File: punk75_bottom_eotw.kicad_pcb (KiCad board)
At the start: 2 copper layers, 285.8 x 124.6 mm, 12 parts

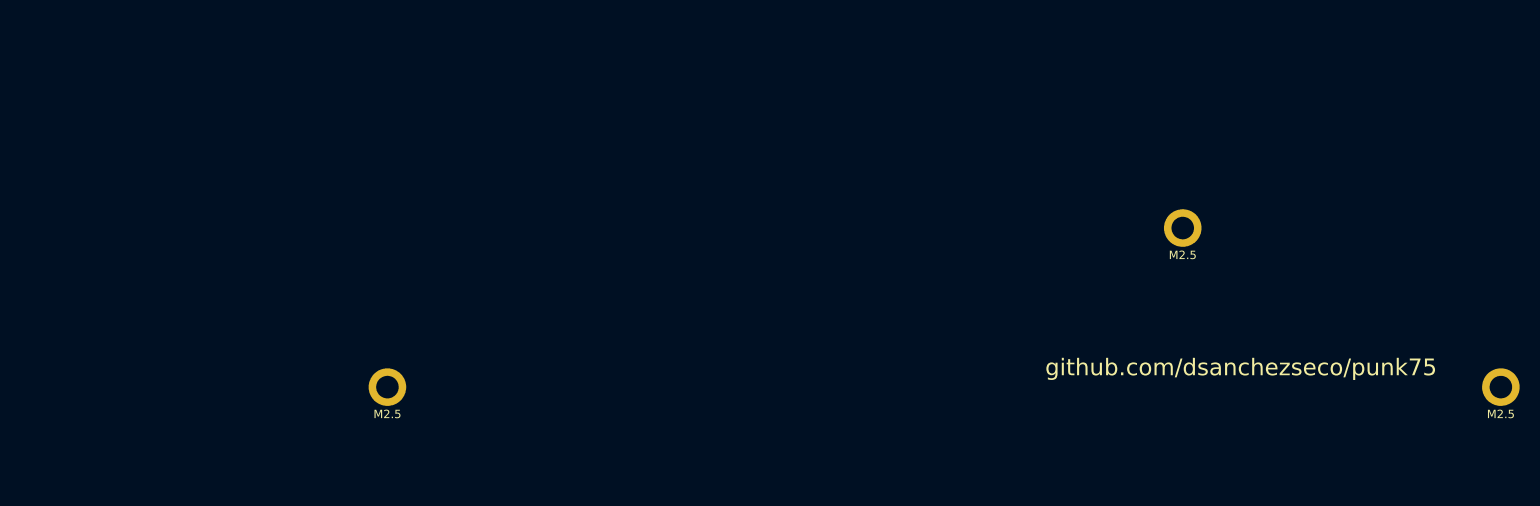
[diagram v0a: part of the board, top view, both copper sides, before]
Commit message: added eotw plate
also fixed straight cuts being two different lines instead of one
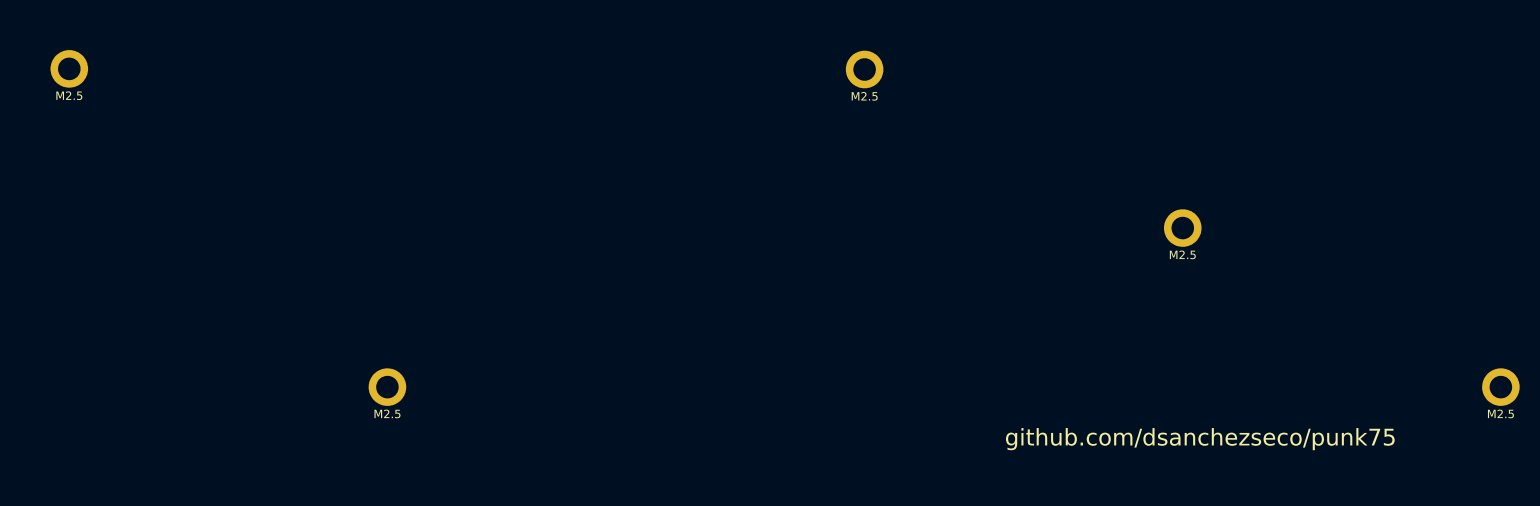
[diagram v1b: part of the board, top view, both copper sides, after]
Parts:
- added H3: M2.5, MountingHole:MountingHole_2.7mm_M2.5_ISO7380_Pad, F.Cu at (269.9, 173.1)
- added H4: M2.5, MountingHole:MountingHole_2.7mm_M2.5_ISO7380_Pad, F.Cu at (174.6, 173.0)
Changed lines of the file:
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@@
     (tracks 0)
     (zones 0)
-    (modules 12)
+    (modules 14)
     (nets 1)
   )
@@
     (36 B.SilkS user)
     (37 F.SilkS user)
-    (38 B.Mask user hide)
-    (39 F.Mask user hide)
+    (38 B.Mask user)
+    (39 F.Mask user)
     (40 Dwgs.User user hide)
     (41 Cmts.User user hide)
@@
   )
   (module MountingHole:MountingHole_2.7mm_M2.5_ISO7380_Pad (layer F.Cu)
+    (at 269.875 173.1)
+    (descr "Mounting Hole 2.7mm, M2.5, ISO7380")
+    (tags "mounting hole 2.7mm m2.5 iso7380")
+    (attr virtual)
+    (fp_text reference H3 (at 0 -3.25) (layer F.Fab)
+      (effects (font (size 1 1) (thickness 0.15)))
+    )
+    (fp_text value M2.5 (at 0 3.25) (layer F.SilkS)
+      (effects (font (size 1 1) (thickness 0.15)))
+    )
+    (fp_circle (center 0 0) (end 2.5 0) (layer F.CrtYd) (width 0.05))
+    (fp_circle (center 0 0) (end 2.25 0) (layer Cmts.User) (width 0.15))
+    (fp_text user %R (at 0.3 0) (layer F.Fab)
+      (effects (font (size 1 1) (thickness 0.15)))
+    )
+    (pad 1 thru_hole circle (at 0 0) (size 4.5 4.5) (drill 2.7) (layers *.Cu *.Mask))
+  )
+  (module MountingHole:MountingHole_2.7mm_M2.5_ISO7380_Pad (layer F.Cu)
+    (at 174.625 173.025)
+    (descr "Mounting Hole 2.7mm, M2.5, ISO7380")
+    (tags "mounting hole 2.7mm m2.5 iso7380")
+    (attr virtual)
+    (fp_text reference H4 (at 0 -3.25) (layer F.Fab)
+      (effects (font (size 1 1) (thickness 0.15)))
+    )
+    (fp_text value M2.5 (at 0 3.25) (layer F.SilkS)
+      (effects (font (size 1 1) (thickness 0.15)))
+    )
+    (fp_circle (center 0 0) (end 2.5 0) (layer F.CrtYd) (width 0.05))
+    (fp_circle (center 0 0) (end 2.25 0) (layer Cmts.User) (width 0.15))
+    (fp_text user %R (at 0.3 0) (layer F.Fab)
+      (effects (font (size 1 1) (thickness 0.15)))
+    )
+    (pad 1 thru_hole circle (at 0 0) (size 4.5 4.5) (drill 2.7) (layers *.Cu *.Mask))
+  )
+  (module MountingHole:MountingHole_2.7mm_M2.5_ISO7380_Pad (layer F.Cu)
     (at 307.975 192.0875)
     (descr "Mounting Hole 2.7mm, M2.5, ISO7380")
@@
     (pad 1 thru_hole circle (at 0 0) (size 4.5 4.5) (drill 2.7) (layers *.Cu *.Mask))
   )
+  (gr_line (start 362.74375 230.1875) (end 81.75625 230.1875) (layer Edge.Cuts) (width 0.05))
+  (gr_arc (start 81.75625 227.80625) (end 79.375 227.80625) (angle -90) (layer Edge.Cuts) (width 0.05))
   (gr_line (start 178.108194 155.849959) (end 177.101994 152.120223) (layer B.SilkS) (width 1))
   (gr_arc (start 173.120175 136.315509) (end 172.861656 136.381036) (angle 53.61851981) (layer B.SilkS) (width 1))
@@
     (effects (font (size 1 1) (thickness 0.15)))
   )
-  (gr_text github.com/dsanchezseco/punk75 (at 314.96 208.788) (layer F.SilkS)
+  (gr_text github.com/dsanchezseco/punk75 (at 310.125 217.2) (layer F.SilkS)
     (effects (font (size 2 2) (thickness 0.15)))
   )
   (gr_line (start 362.74375 105.56875) (end 82.55 105.56875) (layer Edge.Cuts) (width 0.05))
-  (gr_line (start 362.74375 230.1875) (end 81.75625 230.1875) (layer Edge.Cuts) (width 0.05))
   (gr_line (start 365.125 107.95) (end 365.125 227.80625) (layer Edge.Cuts) (width 0.05))
   (gr_arc (start 362.74375 107.95) (end 365.125 107.95) (angle -90) (layer Edge.Cuts) (width 0.05))
@@
   (gr_arc (start 81.75625 107.95) (end 81.75625 105.56875) (angle -90) (layer Edge.Cuts) (width 0.05))
   (gr_line (start 79.375 107.95) (end 79.375 227.80625) (layer Edge.Cuts) (width 0.05))
-  (gr_arc (start 81.75625 227.80625) (end 79.375 227.80625) (angle -90) (layer Edge.Cuts) (width 0.05))
   (gr_arc (start 362.74375 227.80625) (end 362.74375 230.1875) (angle -90) (layer Edge.Cuts) (width 0.05))
   (zone (net 0) (net_name "") (layer B.SilkS) (hatch edge 0.508)
